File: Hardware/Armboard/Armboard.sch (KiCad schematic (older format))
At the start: 0 parts

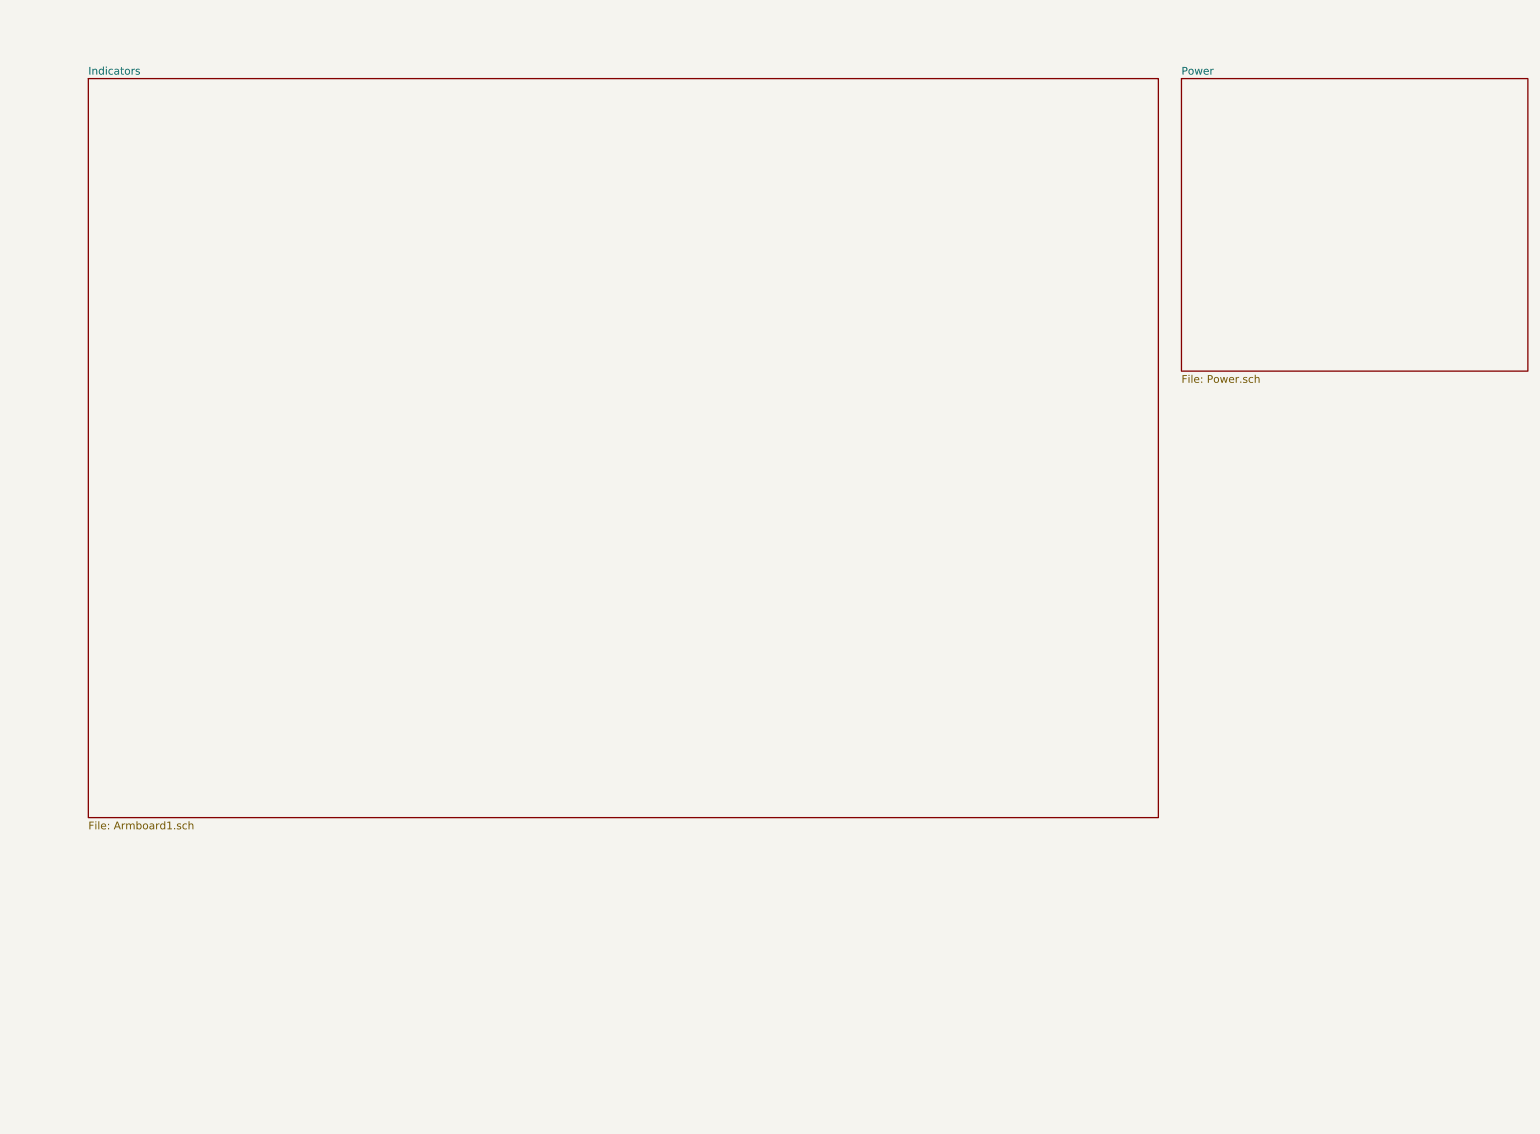
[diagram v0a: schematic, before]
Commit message: Put Anderson connectors on front page, replaced OKI with Buckman converter
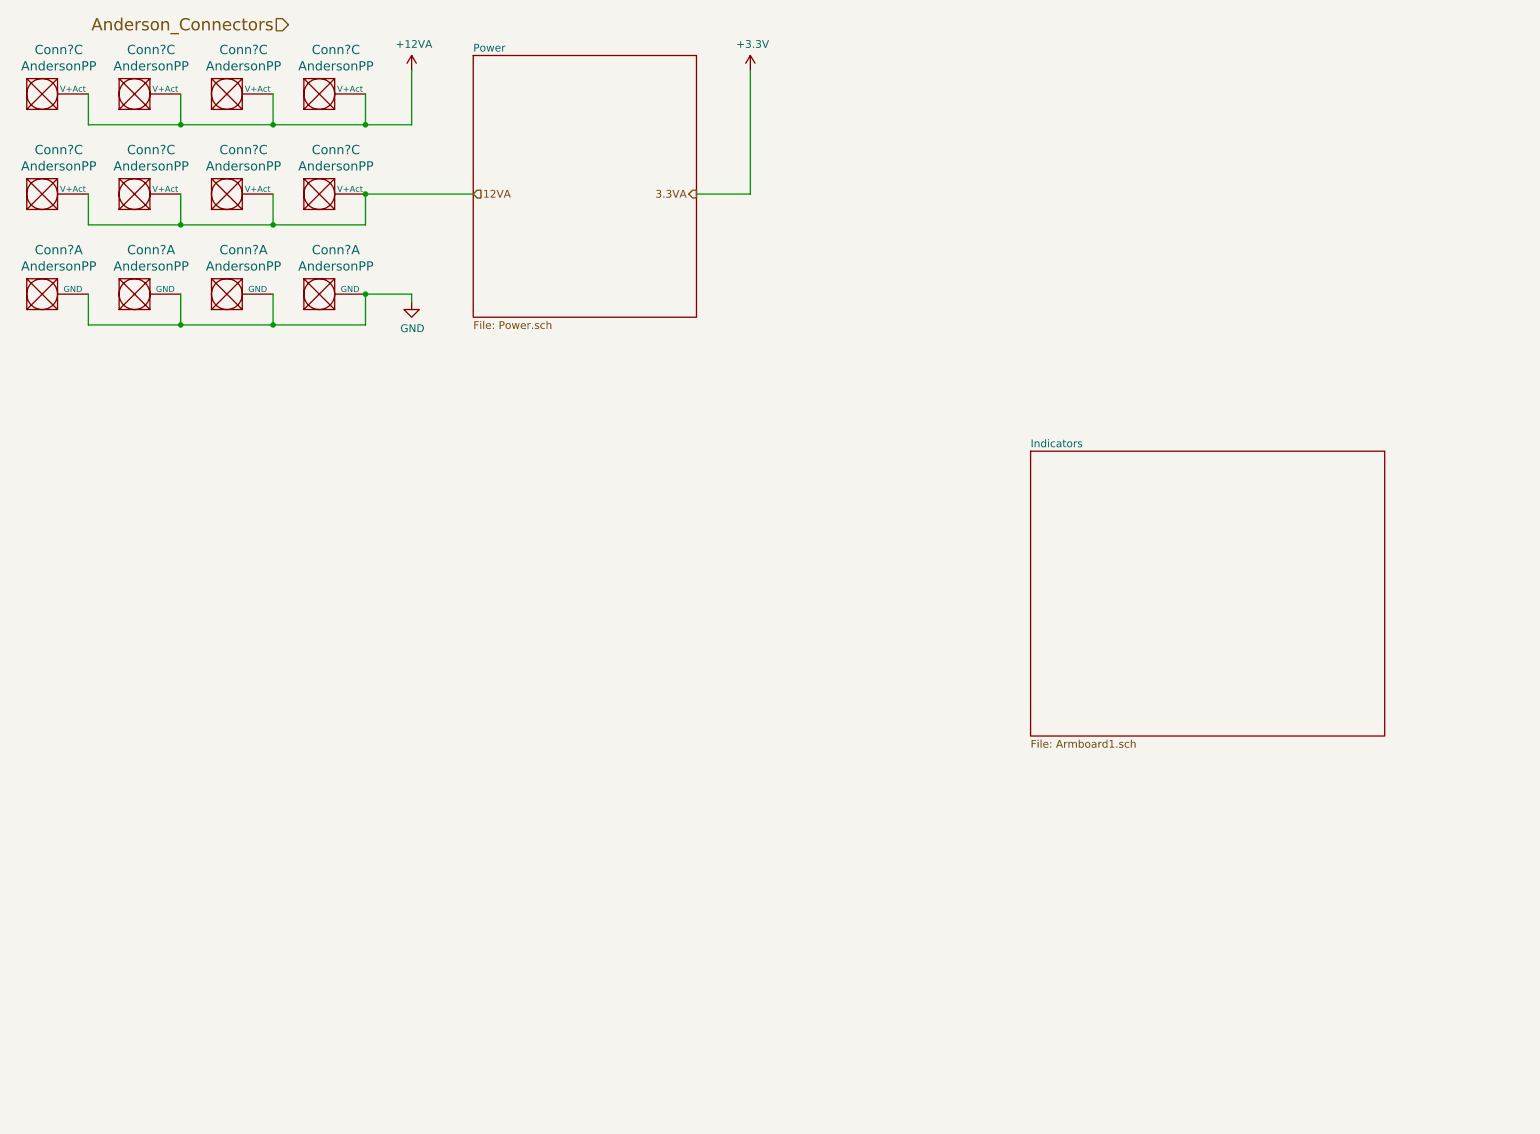
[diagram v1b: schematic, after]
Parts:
- added Conn? (x12): AndersonPP, symbol Armboard-rescue:AndersonPP-MRDT_Connectors-Armboard-rescue
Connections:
- new net +12VA: Conn?.3 (V+Act), Conn?.3 (V+Act), Conn?.3 (V+Act), Conn?.3 (V+Act)
- new net 12VA: Conn?.3 (V+Act), Conn?.3 (V+Act), Conn?.3 (V+Act), Conn?.3 (V+Act)
- new net GND: Conn?.1 (GND), Conn?.1 (GND), Conn?.1 (GND), Conn?.1 (GND)

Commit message: Added empty heirarchical sheets
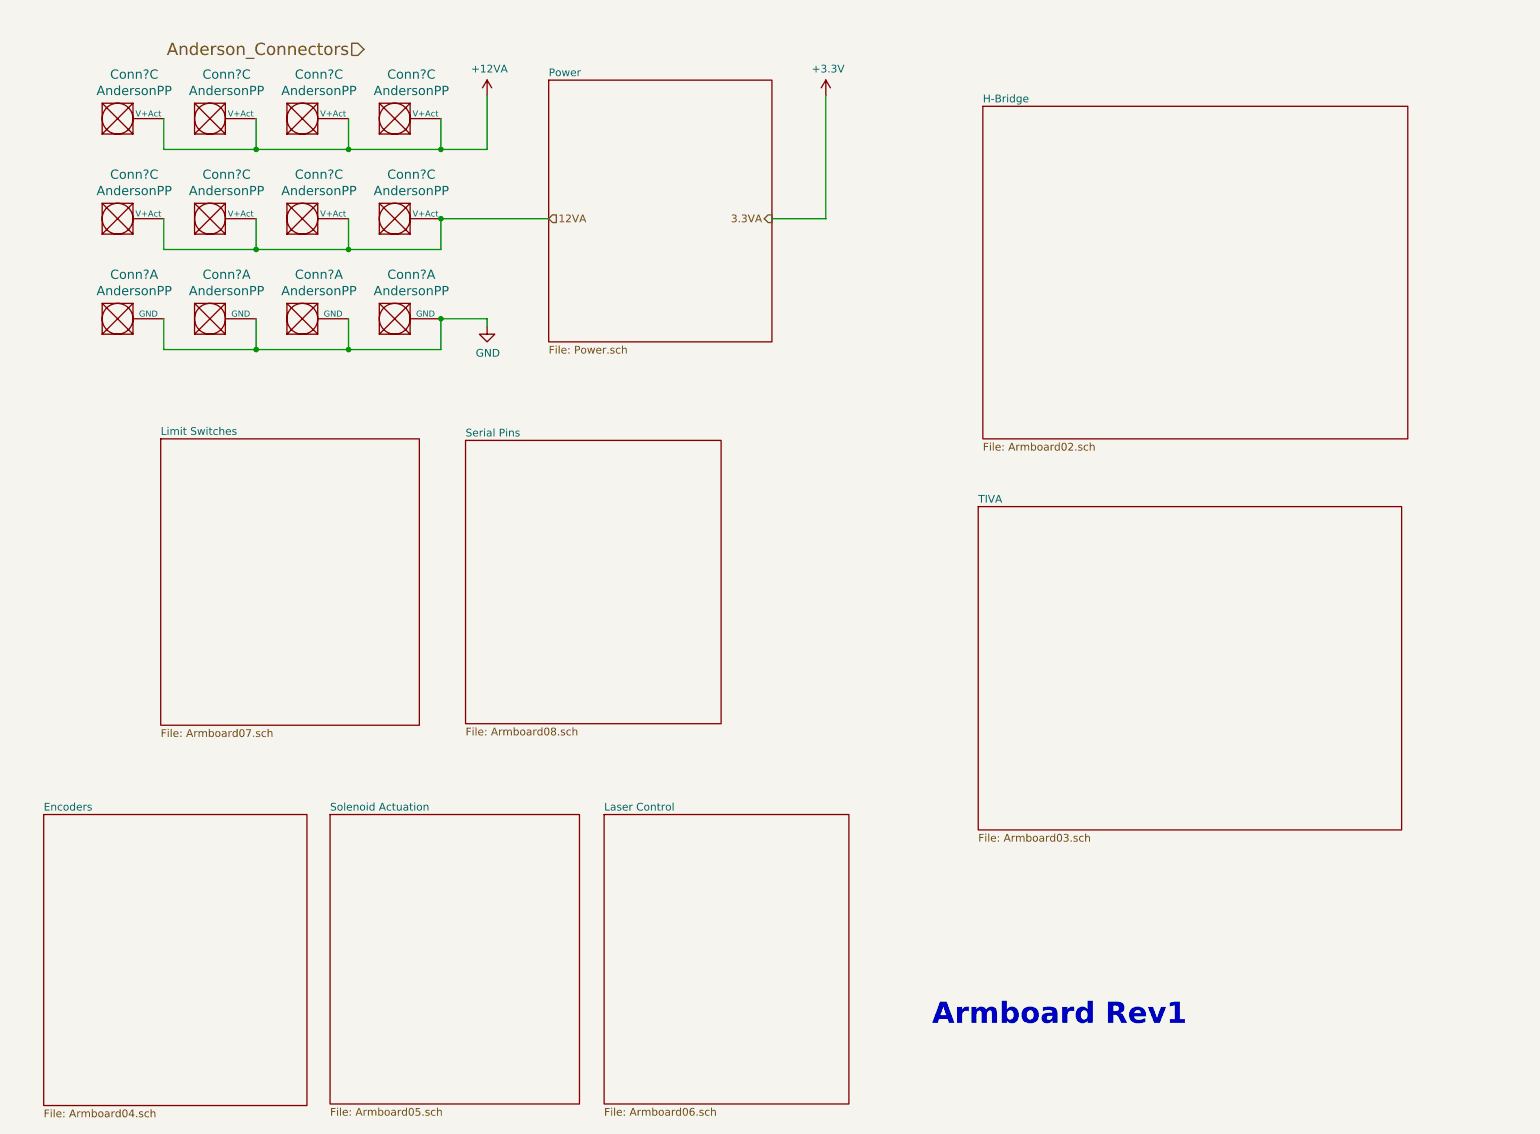
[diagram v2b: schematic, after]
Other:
- note added: "Armboard Rev1"
- moved on the sheet: Conn?A, Conn?C
